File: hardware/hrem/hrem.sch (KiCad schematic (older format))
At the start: 18 parts, among them J1 ICSP, J2 Hall_Conn, Q1 BC547, SW1 SW_Push_Dual, U1 HT7733A, U2 ATtiny85

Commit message: KiCad new footprints
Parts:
- C1: footprint Capacitor_THT:CP_Radial_D5.0mm_P2.50mm -> Capacitor_Tantalum_SMD:CP_EIA-3528-15_AVX-H_Pad1.50x2.35mm_HandSolder; Part (none) -> TAJB476K010RNJ
- C2: footprint Capacitor_THT:CP_Radial_D5.0mm_P2.50mm -> Capacitor_Tantalum_SMD:CP_EIA-3528-15_AVX-H_Pad1.50x2.35mm_HandSolder; Part (none) -> TAJB226K010RNJ
- C3: footprint Capacitor_THT:CP_Radial_D5.0mm_P2.50mm -> Capacitor_SMD:C_0805_2012Metric; Part (none) -> C354369
- D1: value 1N5817 -> SS14-E3/61T; footprint Diode_THT:D_DO-41_SOD81_P10.16mm_Horizontal -> Diode_SMD:D_SMA_Handsoldering; Part (none) -> C47460
- J1: Part (none) -> C262302
- L1: Part (none) -> C113087
- Q1: value BC547 -> MMBT4401-7-F; footprint Package_TO_SOT_THT:TO-92_Inline_Wide -> Package_TO_SOT_SMD:SOT-23_Handsoldering; Part (none) -> C151826
- R1: footprint Resistor_THT:R_Axial_DIN0207_L6.3mm_D2.5mm_P7.62mm_Horizontal -> Resistor_SMD:R_0805_2012Metric_Pad1.15x1.40mm_HandSolder; Part (none) -> C103904
- R2: footprint Resistor_THT:R_Axial_DIN0207_L6.3mm_D2.5mm_P7.62mm_Horizontal -> Resistor_SMD:R_0805_2012Metric_Pad1.15x1.40mm_HandSolder; Part (none) -> C410034
- R3: footprint Resistor_THT:R_Axial_DIN0207_L6.3mm_D2.5mm_P7.62mm_Horizontal -> Resistor_SMD:R_0805_2012Metric_Pad1.15x1.40mm_HandSolder; Part (none) -> C204268
- R4: footprint Resistor_THT:R_Axial_DIN0207_L6.3mm_D2.5mm_P7.62mm_Horizontal -> Resistor_SMD:R_0805_2012Metric_Pad1.15x1.40mm_HandSolder; Part (none) -> C193990
- SW1: footprint hrem:button -> Button_Switch_SMD:SW_Push_1P1T_NO_6x6mm_H9.5mm; symbol Switch:SW_Push_Dual -> Switch:SW_Push; Part (none) -> C224982
- U1: footprint hrem:HT7733 -> Package_TO_SOT_SMD:SOT-23-5_HandSoldering
- U2: footprint Package_DIP:DIP-8_W7.62mm_Socket -> Package_SO:SOIC-8_5.23x5.23mm_P1.27mm
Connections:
- net GND: no longer SW1.3
- net SCK: no longer SW1.4
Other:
- moved on the sheet: D2, R3
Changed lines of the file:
@@
 F 0 "U2" H 6470 2196 50  0000 R CNN
 F 1 "ATtiny85" H 6470 2105 50  0000 R CNN
-F 2 "Package_DIP:DIP-8_W7.62mm_Socket" H 7000 2150 50  0001 C CIN
+F 2 "Package_SO:SOIC-8_5.23x5.23mm_P1.27mm" H 7000 2150 50  0001 C CIN
 F 3 "http://ww1.microchip.com/downloads/en/DeviceDoc/atmel-2586-avr-8-bit-microcontroller-attiny25-attiny45-attiny85_datasheet.pdf" H 7000 2150 50  0001 C CNN
 	1    7000 2150
@@
 F 0 "C1" H 2718 1896 50  0000 L CNN
 F 1 "47uF" H 2718 1805 50  0000 L CNN
-F 2 "Capacitor_THT:CP_Radial_D5.0mm_P2.50mm" H 2638 1700 50  0001 C CNN
-F 3 "~" H 2600 1850 50  0001 C CNN
+F 2 "Capacitor_Tantalum_SMD:CP_EIA-3528-15_AVX-H_Pad1.50x2.35mm_HandSolder" H 2638 1700 50  0001 C CNN
+F 3 "https://datasheet.lcsc.com/szlcsc/AVX-TAJB476K010RNJ_C22036.pdf" H 2600 1850 50  0001 C CNN
+F 4 "TAJB476K010RNJ" H 2600 1850 50  0001 C CNN "Part"
 	1    2600 1850
 	1    0    0    -1
-$EndComp
-$Comp
-L Device:LED_Small D2
-U 1 1 5DA03F1D
-P 9150 1400
-F 0 "D2" H 9150 1195 50  0000 C CNN
-F 1 "LED" H 9150 1286 50  0000 C CNN
-F 2 "LED_THT:LED_D5.0mm" V 9150 1400 50  0001 C CNN
-F 3 "~" V 9150 1400 50  0001 C CNN
-	1    9150 1400
-	-1   0    0    1
 $EndComp
 $Comp
@@
 F 0 "C2" H 4618 1996 50  0000 L CNN
 F 1 "22uF" H 4618 1905 50  0000 L CNN
-F 2 "Capacitor_THT:CP_Radial_D5.0mm_P2.50mm" H 4538 1800 50  0001 C CNN
-F 3 "~" H 4500 1950 50  0001 C CNN
+F 2 "Capacitor_Tantalum_SMD:CP_EIA-3528-15_AVX-H_Pad1.50x2.35mm_HandSolder" H 4538 1800 50  0001 C CNN
+F 3 "https://datasheet.lcsc.com/szlcsc/AVX-TAJB226K010RNJ_C7198.pdf" H 4500 1950 50  0001 C CNN
+F 4 "TAJB226K010RNJ" H 4500 1950 50  0001 C CNN "Part"
 	1    4500 1950
 	1    0    0    -1
@@
 P 3750 1600
 F 0 "D1" H 3750 1384 50  0000 C CNN
-F 1 "1N5817" H 3750 1475 50  0000 C CNN
-F 2 "Diode_THT:D_DO-41_SOD81_P10.16mm_Horizontal" H 3750 1425 50  0001 C CNN
-F 3 "http://www.vishay.com/docs/88525/1n5817.pdf" H 3750 1600 50  0001 C CNN
+F 1 "SS14-E3/61T" H 3750 1475 50  0000 C CNN
+F 2 "Diode_SMD:D_SMA_Handsoldering" H 3750 1425 50  0001 C CNN
+F 3 "https://datasheet.lcsc.com/szlcsc/Vishay-Intertech-SS14-E3-61T_C47460.pdf" H 3750 1600 50  0001 C CNN
+F 4 "C47460" H 3750 1600 50  0001 C CNN "Part"
 	1    3750 1600
 	-1   0    0    1
@@
 	1    0    0    -1
 $EndComp
-$Comp
-L Device:R R3
-U 1 1 5DA9218E
-P 8850 1400
-F 0 "R3" V 8950 1400 50  0000 L CNN
-F 1 "68R" V 8750 1350 50  0000 L CNN
-F 2 "Resistor_THT:R_Axial_DIN0207_L6.3mm_D2.5mm_P7.62mm_Horizontal" V 8780 1400 50  0001 C CNN
-F 3 "~" H 8850 1400 50  0001 C CNN
-	1    8850 1400
-	0    -1   -1   0
-$EndComp
 Wire Wire Line
 	7600 1950 8000 1950
-$Comp
-L power:GND #PWR0107
-U 1 1 5DA944A0
-P 9250 1500
-F 0 "#PWR0107" H 9250 1250 50  0001 C CNN
-F 1 "GND" H 9255 1327 50  0000 C CNN
-F 2 "" H 9250 1500 50  0001 C CNN
-F 3 "" H 9250 1500 50  0001 C CNN
-	1    9250 1500
-	1    0    0    -1
-$EndComp
 $Comp
 L Device:R R2
@@
 F 0 "R2" H 7900 2600 50  0000 L CNN
 F 1 "680R" H 7800 2500 50  0000 L CNN
-F 2 "Resistor_THT:R_Axial_DIN0207_L6.3mm_D2.5mm_P7.62mm_Horizontal" V 7980 2550 50  0001 C CNN
+F 2 "Resistor_SMD:R_0805_2012Metric_Pad1.15x1.40mm_HandSolder" V 7980 2550 50  0001 C CNN
 F 3 "~" H 8050 2550 50  0001 C CNN
+F 4 "C410034" H 8050 2550 50  0001 C CNN "Part"
 	1    8050 2550
 	-1   0    0    1
@@
 F 0 "R1" H 7600 2600 50  0000 L CNN
 F 1 "10K" H 7550 2500 50  0000 L CNN
-F 2 "Resistor_THT:R_Axial_DIN0207_L6.3mm_D2.5mm_P7.62mm_Horizontal" V 7680 2550 50  0001 C CNN
+F 2 "Resistor_SMD:R_0805_2012Metric_Pad1.15x1.40mm_HandSolder" V 7680 2550 50  0001 C CNN
 F 3 "~" H 7750 2550 50  0001 C CNN
+F 4 "C103904" H 7750 2550 50  0001 C CNN "Part"
 	1    7750 2550
 	-1   0    0    1
@@
 RST
 Wire Wire Line
-	9000 1400 9050 1400
-Wire Wire Line
 	8450 2350 8700 2350
 Wire Wire Line
@@
 Wire Wire Line
 	8000 1400 8000 1950
-Wire Wire Line
-	9250 1400 9250 1500
 Wire Wire Line
 	7600 2350 7750 2350
@@
 F 0 "U1" V 3577 2100 50  0000 C CNN
 F 1 "HT7733A" V 3486 2100 50  0000 C CNN
-F 2 "hrem:HT7733" H 3900 2000 50  0001 C CNN
+F 2 "Package_TO_SOT_SMD:SOT-23-5_HandSoldering" H 3900 2000 50  0001 C CNN
 F 3 "https://datasheet.lcsc.com/szlcsc/Holtek-Semicon-HT7733A_C131130.pdf" H 3900 2000 50  0001 C CNN
 	1    3900 2050
@@
 F 1 "100uH" H 2950 1724 50  0000 C CNN
 F 2 "Inductor_THT:L_Axial_L5.3mm_D2.2mm_P7.62mm_Horizontal_Vishay_IM-1" H 2950 1600 50  0001 C CNN
-F 3 "~" H 2950 1600 50  0001 C CNN
+F 3 "https://datasheet.lcsc.com/szlcsc/Murata-Electronics-LQH43CN101K03L_C113087.pdf" H 2950 1600 50  0001 C CNN
+F 4 "C113087" H 2950 1600 50  0001 C CNN "Part"
 	1    2950 1600
 	1    0    0    -1
@@
 P 8050 3050
 F 0 "Q1" V 8285 3050 50  0000 C CNN
-F 1 "BC547" V 8376 3050 50  0000 C CNN
-F 2 "Package_TO_SOT_THT:TO-92_Inline_Wide" H 8250 2975 50  0001 L CIN
-F 3 "http://www.fairchildsemi.com/ds/BC/BC547.pdf" H 8050 3050 50  0001 L CNN
+F 1 "MMBT4401-7-F" V 8376 3050 50  0000 C CNN
+F 2 "Package_TO_SOT_SMD:SOT-23_Handsoldering" H 8250 2975 50  0001 L CIN
+F 3 "https://datasheet.lcsc.com/szlcsc/Diodes-Incorporated-MMBT4401-7-F_C151826.pdf" H 8050 3050 50  0001 L CNN
+F 4 "C151826" V 8050 3050 50  0001 C CNN "Part"
 	1    8050 3050
 	0    1    1    0
@@
 F 0 "C3" V 6448 1400 50  0000 C CNN
 F 1 "100nF" V 6539 1400 50  0000 C CNN
-F 2 "Capacitor_THT:CP_Radial_D5.0mm_P2.50mm" H 6738 1250 50  0001 C CNN
-F 3 "~" H 6700 1400 50  0001 C CNN
+F 2 "Capacitor_SMD:C_0805_2012Metric" H 6738 1250 50  0001 C CNN
+F 3 "https://datasheet.lcsc.com/szlcsc/1902141613_Murata-Electronics-GCJ21BR71H104KA01L_C354369.pdf" H 6700 1400 50  0001 C CNN
+F 4 "C354369" V 6700 1400 50  0001 C CNN "Part"
 	1    6700 1400
 	0    1    1    0
@@
 F 0 "R4" V 8850 3150 50  0000 L CNN
 F 1 "100R" V 8650 3050 50  0000 L CNN
-F 2 "Resistor_THT:R_Axial_DIN0207_L6.3mm_D2.5mm_P7.62mm_Horizontal" V 8680 3150 50  0001 C CNN
+F 2 "Resistor_SMD:R_0805_2012Metric_Pad1.15x1.40mm_HandSolder" V 8680 3150 50  0001 C CNN
 F 3 "~" H 8750 3150 50  0001 C CNN
+F 4 "C193990" H 8750 3150 50  0001 C CNN "Part"
 	1    8750 3150
 	0    -1   -1   0
@@
 L power:GND #PWR0111
 U 1 1 5DDF8B2E
-P 7400 950
-F 0 "#PWR0111" H 7400 700 50  0001 C CNN
-F 1 "GND" H 7405 777 50  0000 C CNN
-F 2 "" H 7400 950 50  0001 C CNN
-F 3 "" H 7400 950 50  0001 C CNN
-	1    7400 950
+P 7300 1400
+F 0 "#PWR0111" H 7300 1150 50  0001 C CNN
+F 1 "GND" H 7305 1227 50  0000 C CNN
+F 2 "" H 7300 1400 50  0001 C CNN
+F 3 "" H 7300 1400 50  0001 C CNN
+	1    7300 1400
 	1    0    0    -1
 $EndComp
@@
 	7600 1850 8900 1850
 Wire Wire Line
-	8000 1400 8700 1400
-Wire Wire Line
 	1850 1600 2600 1600
 $Comp
-L Switch:SW_Push_Dual SW1
+L Switch:SW_Push SW1
 U 1 1 5DE40789
-P 7900 1250
-F 0 "SW1" V 7900 1398 50  0000 L CNN
-F 1 "SW_Push_Dual" V 7945 1398 50  0001 L CNN
-F 2 "hrem:button" H 7900 1450 50  0001 C CNN
-F 3 "~" H 7900 1450 50  0001 C CNN
-	1    7900 1250
-	0    1    1    0
-$EndComp
-Wire Wire Line
-	7900 1450 7900 1550
-Wire Wire Line
-	7900 1550 7700 1550
-Wire Wire Line
-	7700 1550 7700 1450
-Connection ~ 7900 1550
-Wire Wire Line
-	7900 1550 7900 2050
-Wire Wire Line
-	7700 1050 7700 800
-Wire Wire Line
-	7900 1050 7900 800
-Wire Wire Line
-	7900 800  7700 800
-Wire Wire Line
-	7700 800  7400 800
-Wire Wire Line
-	7400 800  7400 950
-Connection ~ 7700 800
+P 7600 1200
+F 0 "SW1" V 7600 1348 50  0000 L CNN
+F 1 "SW_Push_Dual" V 7645 1348 50  0001 L CNN
+F 2 "Button_Switch_SMD:SW_Push_1P1T_NO_6x6mm_H9.5mm" H 7600 1400 50  0001 C CNN
+F 3 "https://datasheet.lcsc.com/szlcsc/Diptronics-DTSM-65N-V-T-R_C224982.pdf" H 7600 1400 50  0001 C CNN
+F 4 "C224982" H 7600 1200 50  0001 C CNN "Part"
+	1    7600 1200
+	1    0    0    -1
+$EndComp
+Wire Wire Line
+	7300 1200 7300 1400
 $Comp
 L Connector_Generic:Conn_02x05_Odd_Even J1
@@
 F 1 "ICSP" H 8400 5776 50  0000 C CNN
 F 2 "Connector_IDC:IDC-Header_2x05_P2.54mm_Vertical" H 8350 5450 50  0001 C CNN
-F 3 "~" H 8350 5450 50  0001 C CNN
+F 3 "https://datasheet.lcsc.com/szlcsc/1811021337_JUSHUO-AFC11-S10ICC-00_C262302.pdf" H 8350 5450 50  0001 C CNN
+F 4 "C262302" H 8350 5450 50  0001 C CNN "Part"
 	1    8350 5450
 	1    0    0    -1
@@
 MISO
 NoConn ~ 8150 5350
+$Comp
+L Device:LED_Small D2
+U 1 1 5DA03F1D
+P 8700 1400
+F 0 "D2" H 8700 1195 50  0000 C CNN
+F 1 "LED" H 8700 1286 50  0000 C CNN
+F 2 "LED_THT:LED_D5.0mm" V 8700 1400 50  0001 C CNN
+F 3 "~" V 8700 1400 50  0001 C CNN
+	1    8700 1400
+	-1   0    0    1
+$EndComp
+Wire Wire Line
+	8850 1400 8800 1400
+Wire Wire Line
+	8850 1400 8850 1450
+$Comp
+L power:GND #PWR0107
+U 1 1 5DA944A0
+P 8850 1450
+F 0 "#PWR0107" H 8850 1200 50  0001 C CNN
+F 1 "GND" H 8855 1277 50  0000 C CNN
+F 2 "" H 8850 1450 50  0001 C CNN
+F 3 "" H 8850 1450 50  0001 C CNN
+	1    8850 1450
+	1    0    0    -1
+$EndComp
+Wire Wire Line
+	8550 1400 8600 1400
+Wire Wire Line
+	8000 1400 8250 1400
+$Comp
+L Device:R R3
+U 1 1 5DA9218E
+P 8400 1400
+F 0 "R3" V 8500 1400 50  0000 L CNN
+F 1 "68R" V 8300 1350 50  0000 L CNN
+F 2 "Resistor_SMD:R_0805_2012Metric_Pad1.15x1.40mm_HandSolder" V 8330 1400 50  0001 C CNN
+F 3 "~" H 8400 1400 50  0001 C CNN
+F 4 "C204268" H 8400 1400 50  0001 C CNN "Part"
+	1    8400 1400
+	0    -1   -1   0
+$EndComp
+Wire Wire Line
+	7300 1200 7400 1200
+Wire Wire Line
+	7900 1200 7800 1200
+Wire Wire Line
+	7900 1200 7900 2050
 $EndSCHEMATC

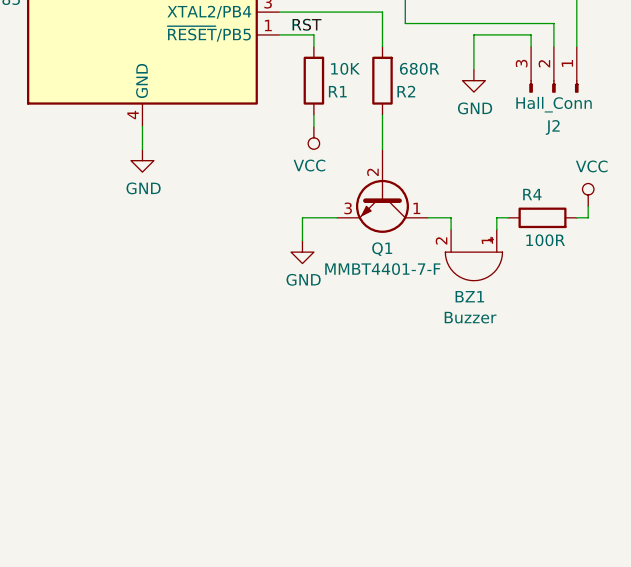
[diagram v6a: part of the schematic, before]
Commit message: Footprint change
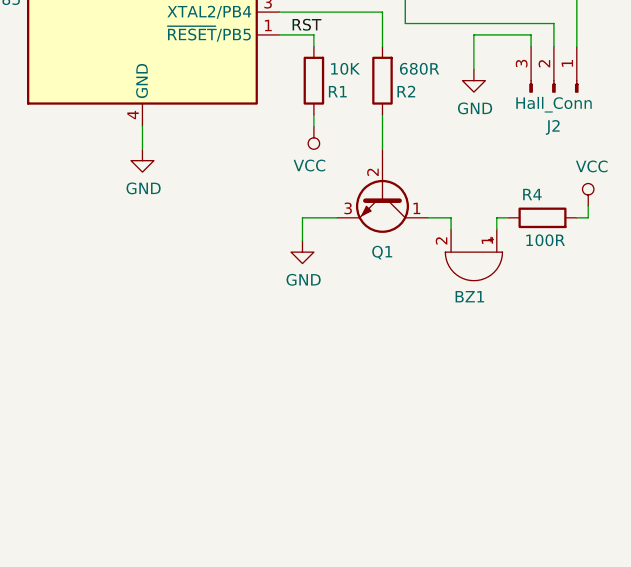
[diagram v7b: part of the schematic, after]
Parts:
- D2: footprint LED_THT:LED_D5.0mm -> LED_THT:LED_D3.0mm
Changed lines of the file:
@@
 P 8450 3300
 F 0 "BZ1" V 8647 3282 50  0000 C CNN
-F 1 "Buzzer" V 8738 3282 50  0000 C CNN
+F 1 "Buzzer" V 8738 3282 50  0001 C CNN
 F 2 "hrem:buzzer" V 8425 3400 50  0001 C CNN
 F 3 "~" V 8425 3400 50  0001 C CNN
@@
 U 1 1 5D9F33C3
 P 8050 3050
-F 0 "Q1" V 8285 3050 50  0000 C CNN
-F 1 "MMBT4401-7-F" V 8376 3050 50  0000 C CNN
+F 0 "Q1" V 8300 3050 50  0000 C CNN
+F 1 "MMBT4401-7-F" V 7950 3450 50  0001 C CNN
 F 2 "Package_TO_SOT_SMD:SOT-23_Handsoldering" H 8250 2975 50  0001 L CIN
 F 3 "https://datasheet.lcsc.com/szlcsc/Diodes-Incorporated-MMBT4401-7-F_C151826.pdf" H 8050 3050 50  0001 L CNN
@@
 F 0 "D2" H 8700 1195 50  0000 C CNN
 F 1 "LED" H 8700 1286 50  0000 C CNN
-F 2 "LED_THT:LED_D5.0mm" V 8700 1400 50  0001 C CNN
+F 2 "LED_THT:LED_D3.0mm" V 8700 1400 50  0001 C CNN
 F 3 "~" V 8700 1400 50  0001 C CNN
 	1    8700 1400

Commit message: Work over schematics
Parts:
- removed J1: ICSP, Connector_IDC:IDC-Header_2x05_P2.54mm_Vertical, symbol Connector_Generic:Conn_02x05_Odd_Even
- added J1: AVR-ISP, Connector_IDC:IDC-Header_2x05_P2.54mm_Vertical, symbol Connector:AVR-ISP-10
- added R5, R6: 0R, Resistor_SMD:R_0805_2012Metric_Pad1.15x1.40mm_HandSolder, symbol Device:R
- added TP1: TestPoint_Flag, TestPoint:TestPoint_Loop_D2.50mm_Drill1.0mm, symbol Connector:TestPoint_Flag
- added TP2, TP3, TP4, TP5: TestPoint_Flag, TestPoint:TestPoint_Pad_D2.0mm, symbol Connector:TestPoint_Flag
- added U3, U4: 74LVC1G125, Package_TO_SOT_SMD:SOT-23-5_HandSoldering, symbol 74xGxx:74LVC1G125
- BT1: footprint Battery:BatteryHolder_Keystone_2466_1xAAA -> hrem:AAA battery
- C3: footprint Capacitor_SMD:C_0805_2012Metric -> Capacitor_SMD:C_0805_2012Metric_Pad1.15x1.40mm_HandSolder
- L1: footprint Inductor_THT:L_Axial_L5.3mm_D2.2mm_P7.62mm_Horizontal_Vishay_IM-1 -> hrem:Murata LQH43
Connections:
- net GND: now also J1.10 (GND), J1.4 (GND), J1.6 (GND), J1.8 (GND), TP1.1, U3.1, U3.3 (GND), U4.1, U4.3 (GND)
- net MISO: now also J1.9 (MISO), R6.1, U3.2; no longer R3.1
- net MOSI: now also J1.1 (MOSI), R5.1, U4.2; no longer J2.1 (Pin_1)
- net RST: now also J1.5 (~RST)
- net SCK: now also J1.7 (SCK)
- net VCC: now also J1.2 (VCC), TP2.1, U3.5 (VCC), U4.5 (VCC)
- net at J2.2 (Pin_2), U2.2 (XTAL1/PB3): now also TP4.1
- net at Q1.2 (B), R2.1: now also TP3.1
- net Vbat: now reaches BT1.1 (+), C1.1, L1.1
- new net: J2.1 (Pin_1), R5.2, TP5.1, U4.4
- new net: R3.1, R6.2, U3.4
- no-connect marks 1 -> 0
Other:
- moved on the sheet: D2, R3
